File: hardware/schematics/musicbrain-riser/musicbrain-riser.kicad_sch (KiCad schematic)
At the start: 2 parts, among them J1 J1, J2 J2

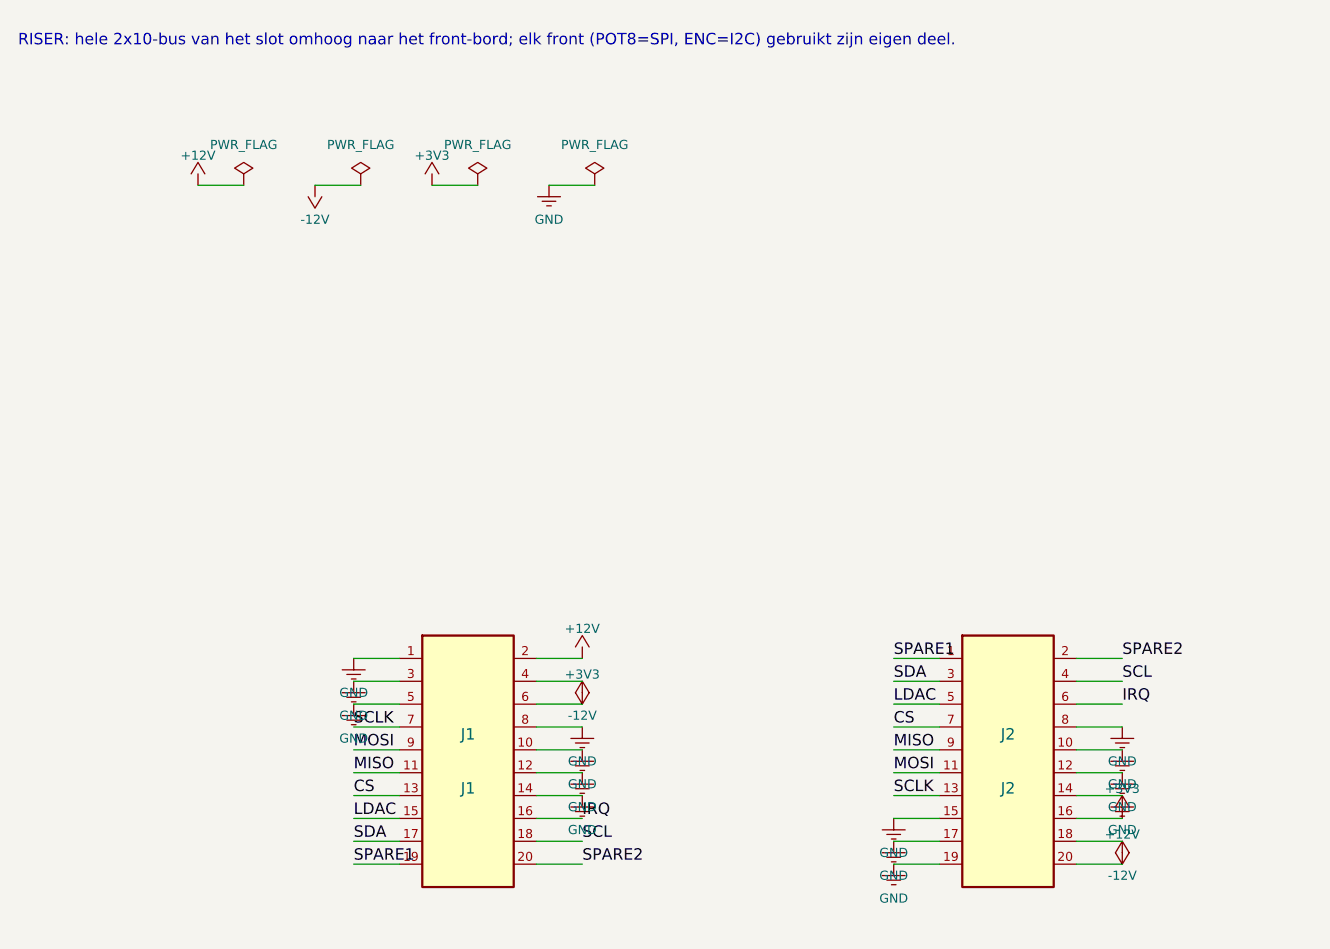
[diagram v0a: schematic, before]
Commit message: Gen 2 stap 3b/3c: riser + potriser rev 2.0 (2x12, H=50) DRC 0/0
riser: 40x50, hele 2x12-bus 1-op-1 omhoog incl. de audio-lijnen ->
ontwikkelbord voor een gedelegeerde Teensy/FPGA. x-matching schaalt mee:
J2-pin q draagt slotfunctie (24-q) oneven / (26-q) even.

potriser: 28x80 -> 80x50, J1 2x12; koper via freerouting i.p.v. handlanen
(1 unrouted -> snap_stubs dichtte 'm). Front-contract 1x10 ongewijzigd.

Meetvondst: de connector-bodies hangen bewust OVER de bordrand (zo mateert
de kaart met de socket eronder) -- dus de vrije kernband bij H=50 is 33,3 mm,
niet 18,8 zoals ik eerst schatte. Daarmee komt elke kaart op 80x50 uit op
5-16% dichtheid (adc8, de drukste: 15,6%) -- lager dan de huidige ~17% op
80 mm hoog. H=50 is dus ruim haalbaar voor alle kaarten.

Alle drie de risers: ERC 0 / netcheck OK / DRC 0/0.

Co-Authored-By: Claude Fable 5 <noreply@anthropic.com>
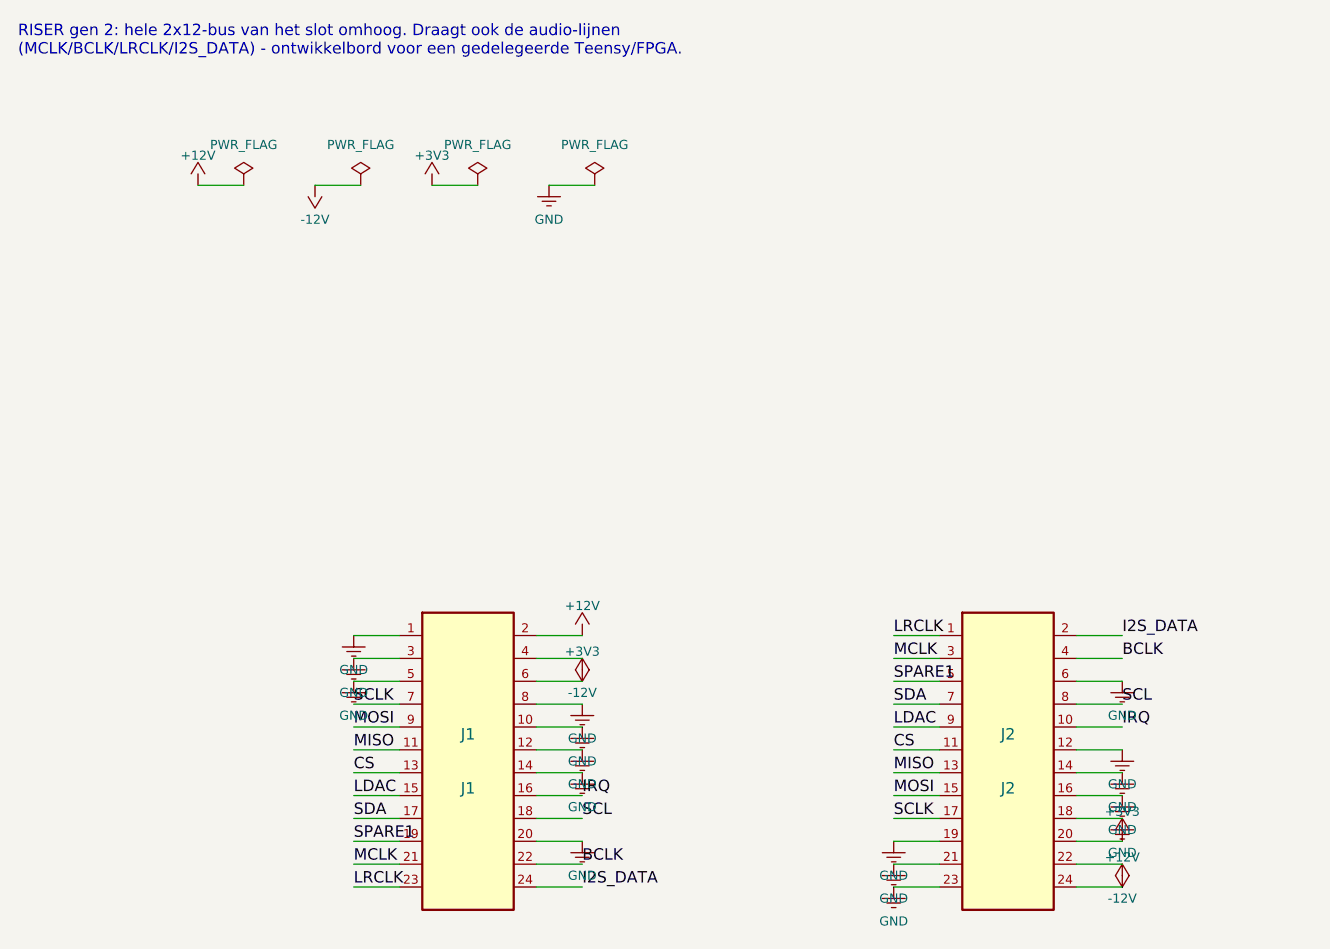
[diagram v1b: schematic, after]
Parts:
- removed J2: J2, Connector_PinHeader_2.54mm:PinHeader_2x10_P2.54mm_Horizontal, symbol Custom:Conn_02x10
- added J2: J2, Connector_PinHeader_2.54mm:PinHeader_2x12_P2.54mm_Horizontal, symbol Custom:Conn_02x12
- J1: footprint Connector_PinHeader_2.54mm:PinHeader_2x10_P2.54mm_Horizontal -> Connector_PinHeader_2.54mm:PinHeader_2x12_P2.54mm_Horizontal; symbol Custom:Conn_02x10 -> Custom:Conn_02x12
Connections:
- net SPARE2 is gone; now on net GND: J1.20 (Pin_20)
- net +12V: now also J2.24 (Pin_24)
- net +3V3: now also J2.20 (Pin_20)
- net -12V: now also J2.22 (Pin_22)
- net CS: now also J2.11 (Pin_11)
- net GND: now also J2.12 (Pin_12), J2.14 (Pin_14), J2.16 (Pin_16), J2.18 (Pin_18), J2.19 (Pin_19), J2.21 (Pin_21), J2.23 (Pin_23), J2.6 (Pin_6)
- net IRQ: now also J2.10 (Pin_10)
- net LDAC: now also J2.9 (Pin_9)
- net MISO: now also J2.13 (Pin_13)
- net MOSI: now also J2.15 (Pin_15)
- net SCL: now also J2.8 (Pin_8)
- net SCLK: now also J2.17 (Pin_17)
- net SDA: now also J2.7 (Pin_7)
- net SPARE1: now also J2.5 (Pin_5)
- new net BCLK: J1.22 (Pin_22), J2.4 (Pin_4)
- new net I2S_DATA: J1.24 (Pin_24), J2.2 (Pin_2)
- new net LRCLK: J1.23 (Pin_23), J2.1 (Pin_1)
- new net MCLK: J1.21 (Pin_21), J2.3 (Pin_3)
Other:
- note added: "RISER gen 2: hele 2x12-bus van het slot omhoog. Draagt ook de audio-lijnen (MCLK/BCLK/LRCLK/I2S_DATA) - ontwikkelbord voor een gedelegeerde Teensy/FPGA."
- note removed: "RISER: hele 2x10-bus van het slot omhoog naar het front-bord; elk front (POT8=SPI, ENC=I2C) gebruikt zijn eigen deel."
- title: MusicBrain RISER - slot-verlenger 2x10 -> MusicBrain RISER - slot-verlenger 2x12
